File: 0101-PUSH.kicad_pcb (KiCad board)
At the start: 2 copper layers, 24.6 x 19.6 mm, 11 parts, among them J1 Conn_01x03, SW1 PUSH

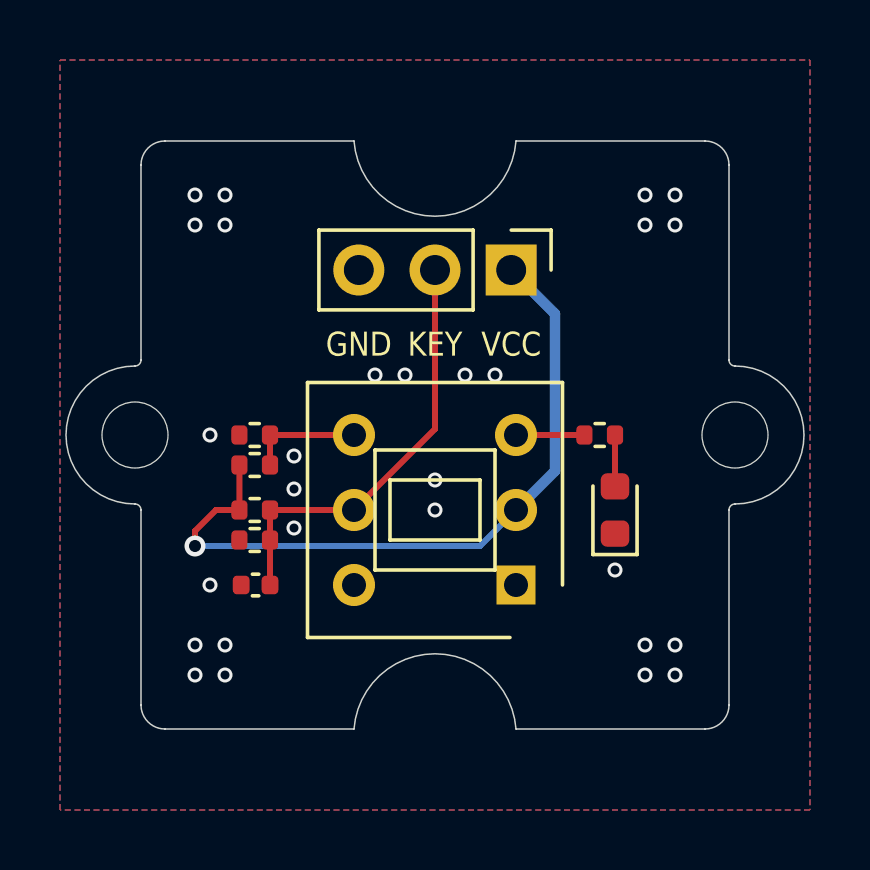
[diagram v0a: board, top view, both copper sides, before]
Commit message: Migrate to KiCad 6
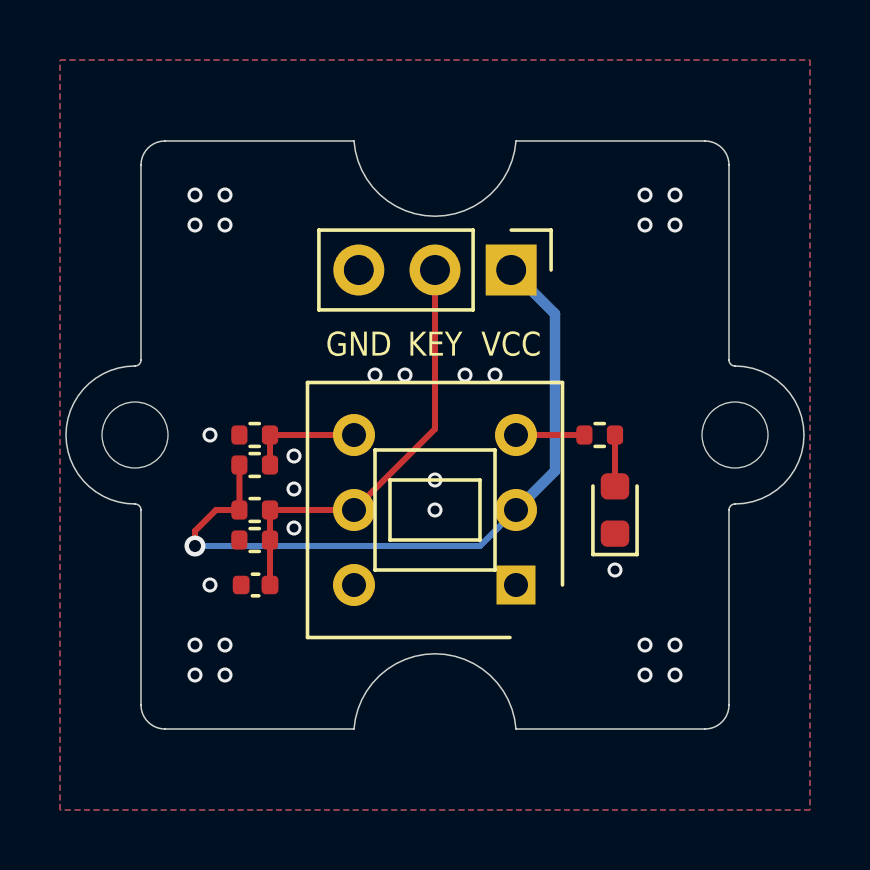
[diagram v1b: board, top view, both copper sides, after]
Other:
- net class Default removed
- net class RF removed
- net class VCC removed

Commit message: Finish
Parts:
- C1: value 0.1uF -> 0.1uF(NC)
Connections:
- SW1 pad 1: (no net) -> unconnected-(SW1-Pad1)
- SW1 pad 4: (no net) -> unconnected-(SW1-Pad4)
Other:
- board text added: "#0101 PUSH V1.0"
- board text added: "JLCJLCJLCJLC"

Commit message: Use kibuzzard silk
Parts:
- added kibuzzard-631DB129: G***, kibuzzard-631DB129, F.Cu at (110.0, 106.8)
- added kibuzzard-631DDDB8: G***, kibuzzard-631DDDB8, F.Cu at (103.5, 101.5)
- added kibuzzard-631DDE16: G***, kibuzzard-631DDE16, F.Cu at (102.5, 118.5)
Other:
- board text added: "PUSH"
- board text removed: "GND"
- board text removed: "KEY"
- board text removed: "VCC"

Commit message: Update PCB settings
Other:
- board text removed: "#0101 PUSH V1.0"
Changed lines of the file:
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@@
   )
   (setup
+    (stackup
+      (layer "F.SilkS" (type "Top Silk Screen") (color "White"))
+      (layer "F.Paste" (type "Top Solder Paste"))
+      (layer "F.Mask" (type "Top Solder Mask") (color "Purple") (thickness 0.01))
+      (layer "F.Cu" (type "copper") (thickness 0.035))
+      (layer "dielectric 1" (type "core") (thickness 1.11) (material "FR4") (epsilon_r 4.5) (loss_tangent 0.02))
+      (layer "B.Cu" (type "copper") (thickness 0.035))
+      (layer "B.Mask" (type "Bottom Solder Mask") (color "Purple") (thickness 0.01))
+      (layer "B.Paste" (type "Bottom Solder Paste"))
+      (layer "B.SilkS" (type "Bottom Silk Screen") (color "White"))
+      (copper_finish "None")
+      (dielectric_constraints no)
+    )
     (pad_to_mask_clearance 0.05)
     (solder_mask_min_width 0.1)
@@
     (pad "2" smd roundrect (at 0.48 0 180) (size 0.56 0.62) (layers "F.Cu" "F.Paste" "F.Mask") (roundrect_rratio 0.25)
       (net 1 "GND") (pintype "passive"))
-    (model "${KICAD6_3DMODEL_DIR}/Capacitor_SMD.3dshapes/C_0402_1005Metric.wrl"
+    (model "${KICAD6_3DMODEL_DIR}/Capacitor_SMD.3dshapes/C_0402_1005Metric.step"
       (offset (xyz 0 0 0))
       (scale (xyz 1 1 1))
@@
     (pad "2" smd roundrect (at 0.7875 0 90) (size 0.875 0.95) (layers "F.Cu" "F.Paste" "F.Mask") (roundrect_rratio 0.25)
       (net 3 "Net-(D1-Pad2)") (pinfunction "A") (pintype "passive"))
-    (model "${KICAD6_3DMODEL_DIR}/LED_SMD.3dshapes/LED_0603_1608Metric.wrl"
+    (model "${KICAD6_3DMODEL_DIR}/LED_SMD.3dshapes/LED_0603_1608Metric.step"
       (offset (xyz 0 0 0))
       (scale (xyz 1 1 1))
@@
     (pad "3" thru_hole oval (at 0 5.08 270) (size 1.7 1.7) (drill 1) (layers *.Cu *.Mask)
       (net 1 "GND") (pinfunction "Pin_3") (pintype "passive"))
-    (model "${KICAD6_3DMODEL_DIR}/Connector_PinHeader_2.54mm.3dshapes/PinHeader_1x03_P2.54mm_Vertical.wrl"
+    (model "${KICAD6_3DMODEL_DIR}/Connector_PinHeader_2.54mm.3dshapes/PinHeader_1x03_P2.54mm_Vertical.step"
       (offset (xyz 0 0 0))
       (scale (xyz 1 1 1))
@@
     (pad "2" smd roundrect (at 0.51 0) (size 0.54 0.64) (layers "F.Cu" "F.Paste" "F.Mask") (roundrect_rratio 0.25)
       (net 2 "/KEY") (pintype "passive"))
-    (model "${KICAD6_3DMODEL_DIR}/Resistor_SMD.3dshapes/R_0402_1005Metric.wrl"
+    (model "${KICAD6_3DMODEL_DIR}/Resistor_SMD.3dshapes/R_0402_1005Metric.step"
       (offset (xyz 0 0 0))
       (scale (xyz 1 1 1))
@@
     (pad "2" smd roundrect (at 0.51 0 180) (size 0.54 0.64) (layers "F.Cu" "F.Paste" "F.Mask") (roundrect_rratio 0.25)
       (net 1 "GND") (pintype "passive"))
-    (model "${KICAD6_3DMODEL_DIR}/Resistor_SMD.3dshapes/R_0402_1005Metric.wrl"
+    (model "${KICAD6_3DMODEL_DIR}/Resistor_SMD.3dshapes/R_0402_1005Metric.step"
       (offset (xyz 0 0 0))
       (scale (xyz 1 1 1))
@@
     (pad "2" smd roundrect (at 0.51 0) (size 0.54 0.64) (layers "F.Cu" "F.Paste" "F.Mask") (roundrect_rratio 0.25)
       (net 5 "Net-(R3-Pad2)") (pintype "passive"))
-    (model "${KICAD6_3DMODEL_DIR}/Resistor_SMD.3dshapes/R_0402_1005Metric.wrl"
+    (model "${KICAD6_3DMODEL_DIR}/Resistor_SMD.3dshapes/R_0402_1005Metric.step"
       (offset (xyz 0 0 0))
       (scale (xyz 1 1 1))
@@
     (pad "2" smd roundrect (at 0.51 0 180) (size 0.54 0.64) (layers "F.Cu" "F.Paste" "F.Mask") (roundrect_rratio 0.25)
       (net 1 "GND") (pintype "passive"))
-    (model "${KICAD6_3DMODEL_DIR}/Resistor_SMD.3dshapes/R_0402_1005Metric.wrl"
+    (model "${KICAD6_3DMODEL_DIR}/Resistor_SMD.3dshapes/R_0402_1005Metric.step"
       (offset (xyz 0 0 0))
       (scale (xyz 1 1 1))
@@
     (pad "2" smd roundrect (at 0.51 0 180) (size 0.54 0.64) (layers "F.Cu" "F.Paste" "F.Mask") (roundrect_rratio 0.25)
       (net 6 "Net-(R5-Pad2)") (pintype "passive"))
-    (model "${KICAD6_3DMODEL_DIR}/Resistor_SMD.3dshapes/R_0402_1005Metric.wrl"
+    (model "${KICAD6_3DMODEL_DIR}/Resistor_SMD.3dshapes/R_0402_1005Metric.step"
       (offset (xyz 0 0 0))
       (scale (xyz 1 1 1))
@@
   (gr_arc (start 100.2 101) (mid 100.434315 100.434315) (end 101 100.2) (layer "Edge.Cuts") (width 0.05))
   (gr_arc (start 120 107.699999) (mid 119.858579 107.641421) (end 119.800001 107.5) (layer "Edge.Cuts") (width 0.05))
-  (gr_text "#0101 PUSH\nV1.0" (at 115 107.5) (layer "B.SilkS")
-    (effects (font (size 1 1) (thickness 0.15)) (justify left mirror))
-  )
   (gr_text "JLCJLCJLCJLC" (at 110 116.5) (layer "B.SilkS")
     (effects (font (size 0.8 0.8) (thickness 0.12)) (justify mirror))

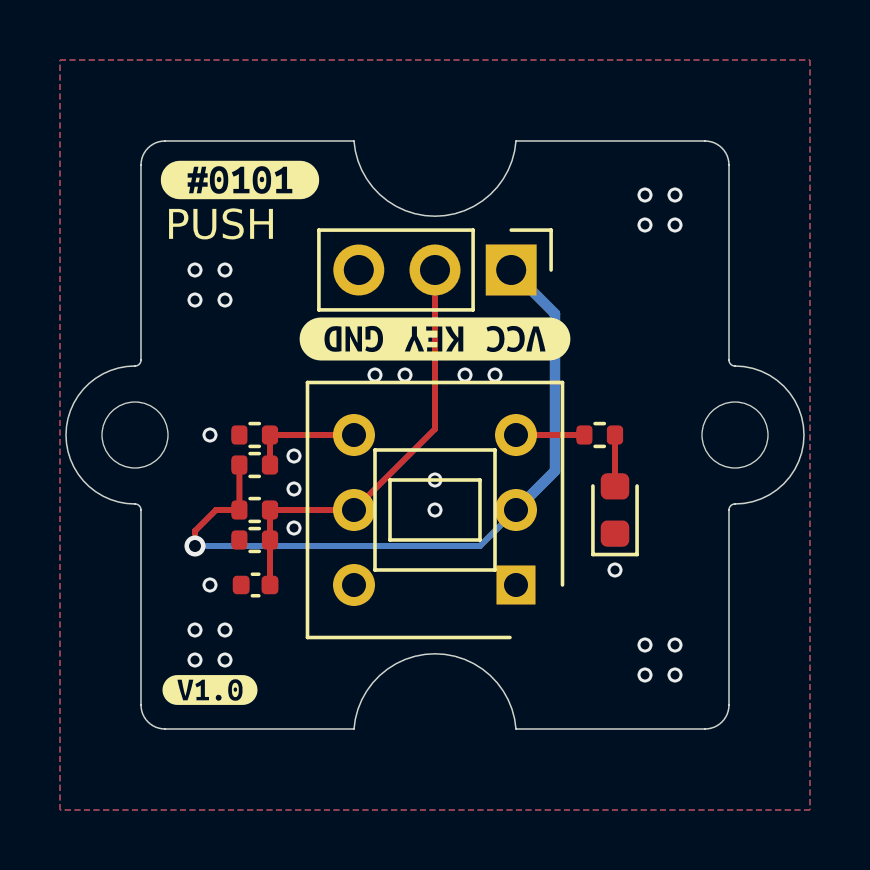
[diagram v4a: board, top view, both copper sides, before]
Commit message: Update pull-up/down resistors
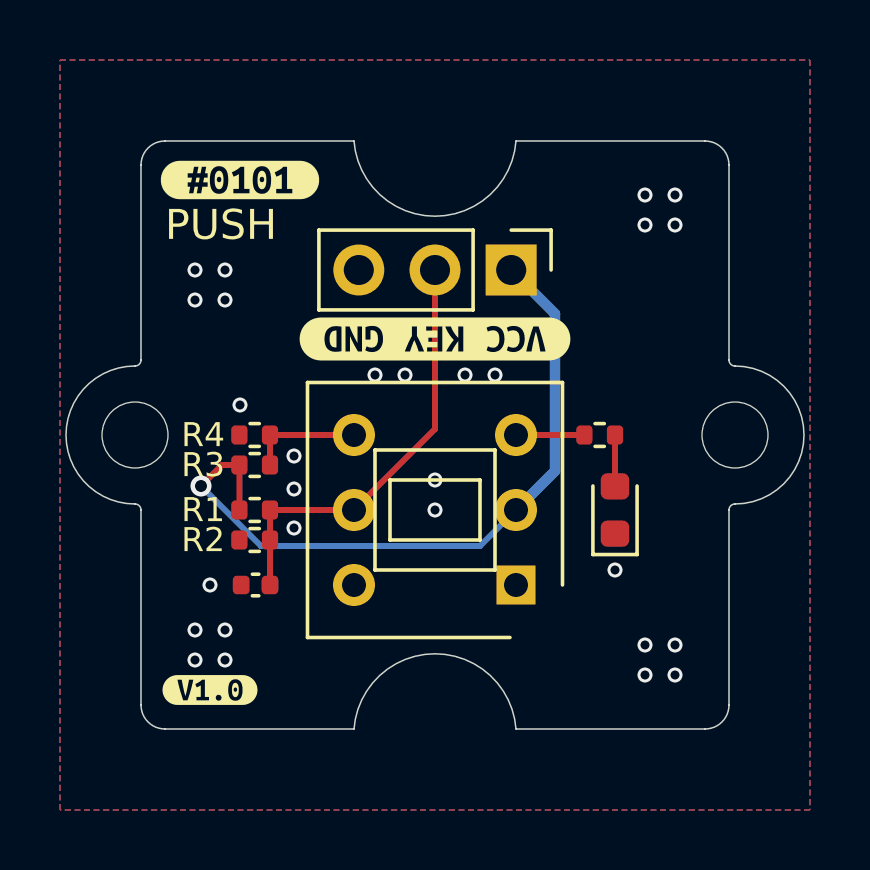
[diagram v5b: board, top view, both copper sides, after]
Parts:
- R1: value 10K(NC) -> 10K
- R4: value 0R(NC) -> 0R
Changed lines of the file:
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@@
     (descr "Resistor SMD 0402 (1005 Metric), square (rectangular) end terminal, IPC_7351 nominal, (Body size source: IPC-SM-782 page 72, https://www.pcb-3d.com/wordpress/wp-content/uploads/ipc-sm-782a_amendment_1_and_2.pdf), generated with kicad-footprint-generator")
     (tags "resistor")
-    (property "Manufacturer" "~")
-    (property "PartNumber" "~")
+    (property "Manufacturer" "UniOhm")
+    (property "PartNumber" "C25744")
     (property "Sheetfile" "0101-PUSH.kicad_sch")
     (property "Sheetname" "")
-    (property "Supplier" "~")
+    (property "Supplier" "JLC")
     (attr smd)
-    (fp_text reference "R1" (at 0 -1.17) (layer "F.SilkS") hide
-      (effects (font (size 1 1) (thickness 0.15)))
-    )
-    (fp_text value "10K(NC)" (at 0 1.17) (layer "F.Fab")
+    (fp_text reference "R1" (at -0.99 0) (layer "F.SilkS")
+      (effects (font (size 0.8 0.8) (thickness 0.12)) (justify right))
+    )
+    (fp_text value "10K" (at 0 1.17) (layer "F.Fab")
       (effects (font (size 1 1) (thickness 0.15)))
     )
@@
     (property "Supplier" "~")
     (attr smd)
-    (fp_text reference "R2" (at 0 -1.17) (layer "F.SilkS") hide
-      (effects (font (size 1 1) (thickness 0.15)))
+    (fp_text reference "R2" (at 0.99 0) (layer "F.SilkS")
+      (effects (font (size 0.8 0.8) (thickness 0.12)) (justify right))
     )
     (fp_text value "10K(NC)" (at 0 1.17) (layer "F.Fab")
@@
     (pad "2" smd roundrect (at 0.51 0 180) (size 0.54 0.64) (layers "F.Cu" "F.Paste" "F.Mask") (roundrect_rratio 0.25)
       (net 1 "GND") (pintype "passive"))
-    (model "${KICAD6_3DMODEL_DIR}/Resistor_SMD.3dshapes/R_0402_1005Metric.step"
-      (offset (xyz 0 0 0))
-      (scale (xyz 1 1 1))
-      (rotate (xyz 0 0 0))
-    )
   )
   (footprint "Resistor_SMD:R_0402_1005Metric" (layer "F.Cu")
@@
     (property "Supplier" "~")
     (attr smd)
-    (fp_text reference "R3" (at 0 -1.17) (layer "F.SilkS") hide
-      (effects (font (size 1 1) (thickness 0.15)))
+    (fp_text reference "R3" (at -0.99 0) (layer "F.SilkS")
+      (effects (font (size 0.8 0.8) (thickness 0.12)) (justify right))
     )
     (fp_text value "0R(NC)" (at 0 1.17) (layer "F.Fab")
@@
     (pad "2" smd roundrect (at 0.51 0) (size 0.54 0.64) (layers "F.Cu" "F.Paste" "F.Mask") (roundrect_rratio 0.25)
       (net 5 "Net-(R3-Pad2)") (pintype "passive"))
-    (model "${KICAD6_3DMODEL_DIR}/Resistor_SMD.3dshapes/R_0402_1005Metric.step"
-      (offset (xyz 0 0 0))
-      (scale (xyz 1 1 1))
-      (rotate (xyz 0 0 0))
-    )
   )
   (footprint "Resistor_SMD:R_0402_1005Metric" (layer "F.Cu")
@@
     (descr "Resistor SMD 0402 (1005 Metric), square (rectangular) end terminal, IPC_7351 nominal, (Body size source: IPC-SM-782 page 72, https://www.pcb-3d.com/wordpress/wp-content/uploads/ipc-sm-782a_amendment_1_and_2.pdf), generated with kicad-footprint-generator")
     (tags "resistor")
-    (property "Manufacturer" "~")
-    (property "PartNumber" "~")
+    (property "Manufacturer" "UniOhm")
+    (property "PartNumber" "C17168")
     (property "Sheetfile" "0101-PUSH.kicad_sch")
     (property "Sheetname" "")
-    (property "Supplier" "~")
+    (property "Supplier" "JLC")
     (attr smd)
-    (fp_text reference "R4" (at 0 -1.17) (layer "F.SilkS") hide
-      (effects (font (size 1 1) (thickness 0.15)))
-    )
-    (fp_text value "0R(NC)" (at 0 1.17) (layer "F.Fab")
+    (fp_text reference "R4" (at 0.99 0) (layer "F.SilkS")
+      (effects (font (size 0.8 0.8) (thickness 0.12)) (justify right))
+    )
+    (fp_text value "0R" (at 0 1.17) (layer "F.Fab")
       (effects (font (size 1 1) (thickness 0.15)))
     )
@@
   (via (at 105.3 110.7) (size 0.5) (drill 0.3) (layers "F.Cu" "B.Cu") (net 1))
   (via (at 116 114.5) (size 0.5) (drill 0.3) (layers "F.Cu" "B.Cu") (net 1))
-  (via (at 102.5 110) (size 0.5) (drill 0.3) (layers "F.Cu" "B.Cu") (net 1))
+  (via (at 103.5 109) (size 0.5) (drill 0.3) (layers "F.Cu" "B.Cu") (net 1))
   (via (at 102 105.5) (size 0.5) (drill 0.3) (layers "F.Cu" "B.Cu") (free) (net 1))
   (via (at 102 117.5) (size 0.5) (drill 0.3) (layers "F.Cu" "B.Cu") (net 1))
@@
   (segment (start 104.5 112.5) (end 104.5 115) (width 0.2) (layer "F.Cu") (net 2))
   (segment (start 116 111.7125) (end 116 110) (width 0.2) (layer "F.Cu") (net 3))
-  (segment (start 102 113.2) (end 102.7 112.5) (width 0.2) (layer "F.Cu") (net 4))
-  (segment (start 102 113.7) (end 102 113.2) (width 0.2) (layer "F.Cu") (net 4))
-  (segment (start 102.7 112.5) (end 103.48 112.5) (width 0.2) (layer "F.Cu") (net 4))
+  (segment (start 103.48 111) (end 102.9 111) (width 0.2) (layer "F.Cu") (net 4))
+  (segment (start 102.9 111) (end 102.2 111.7) (width 0.2) (layer "F.Cu") (net 4))
   (segment (start 103.48 112.5) (end 103.48 111) (width 0.2) (layer "F.Cu") (net 4))
-  (via (at 102 113.7) (size 0.7) (drill 0.4) (layers "F.Cu" "B.Cu") (net 4))
+  (via (at 102.2 111.7) (size 0.7) (drill 0.4) (layers "F.Cu" "B.Cu") (net 4))
+  (segment (start 111.5 113.7) (end 112.7 112.5) (width 0.2) (layer "B.Cu") (net 4))
+  (segment (start 104.2 113.7) (end 111.5 113.7) (width 0.2) (layer "B.Cu") (net 4))
   (segment (start 112.7 112.5) (end 114 111.2) (width 0.35) (layer "B.Cu") (net 4))
-  (segment (start 111.5 113.7) (end 102 113.7) (width 0.2) (layer "B.Cu") (net 4))
-  (segment (start 112.7 112.5) (end 111.5 113.7) (width 0.2) (layer "B.Cu") (net 4))
   (segment (start 114 105.96) (end 112.54 104.5) (width 0.35) (layer "B.Cu") (net 4))
+  (segment (start 102.2 111.7) (end 104.2 113.7) (width 0.2) (layer "B.Cu") (net 4))
   (segment (start 114 111.2) (end 114 105.96) (width 0.35) (layer "B.Cu") (net 4))
   (segment (start 107.3 110) (end 104.5 110) (width 0.2) (layer "F.Cu") (net 5))
